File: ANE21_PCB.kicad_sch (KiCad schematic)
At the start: 8 parts

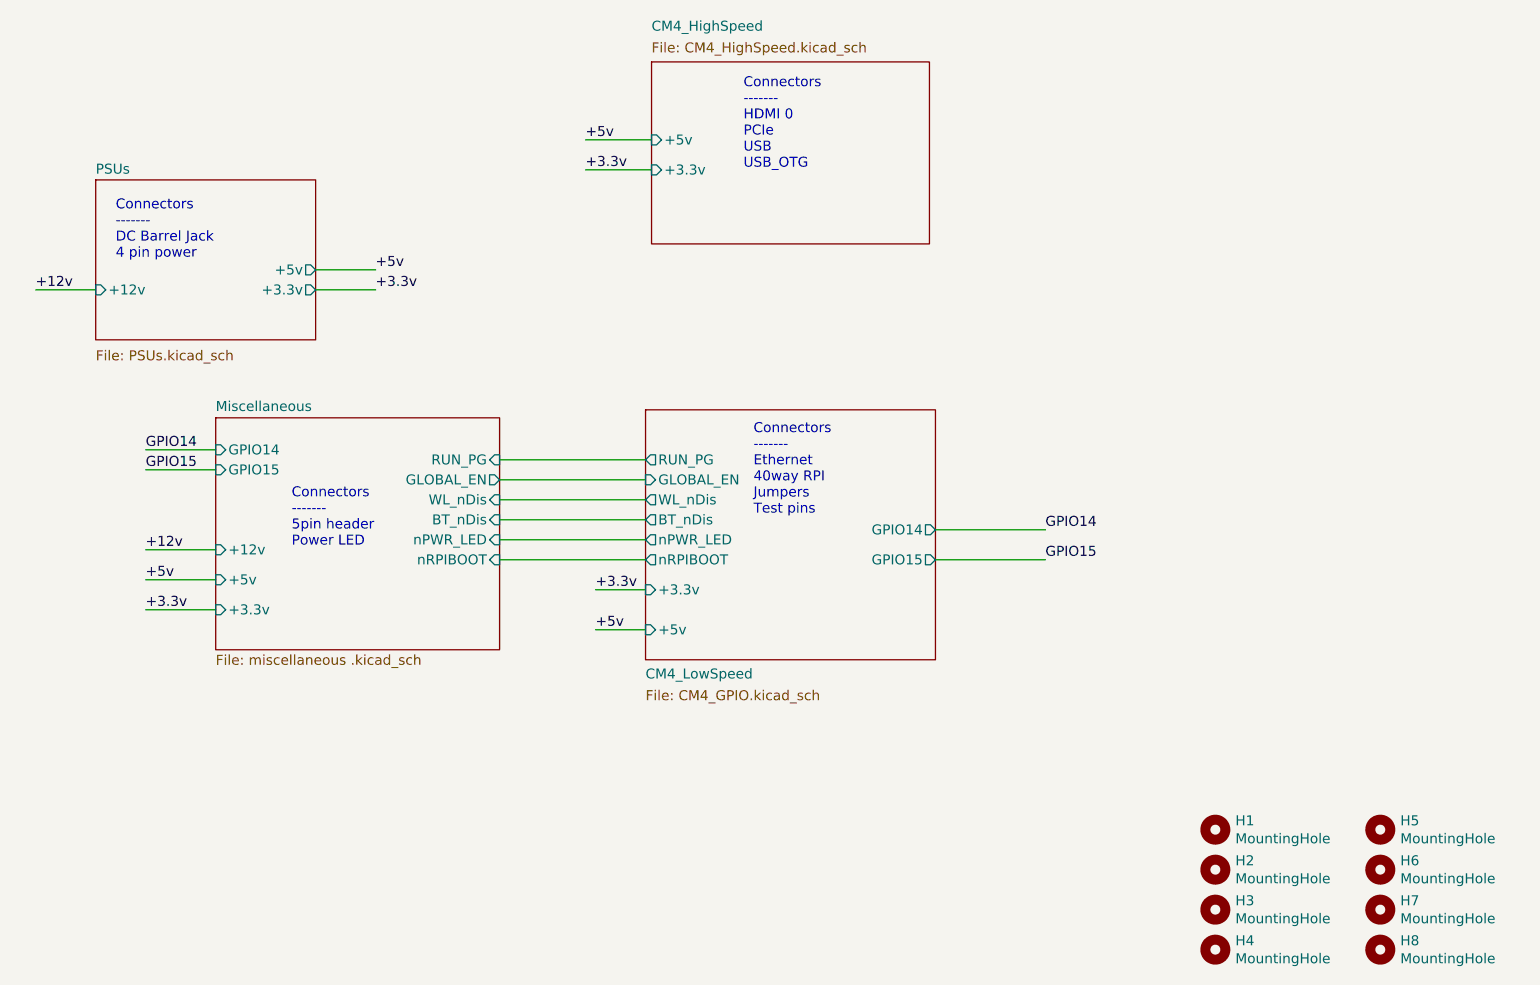
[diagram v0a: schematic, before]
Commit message: Adjusted 3.3v for CM4 3.3v output, PCIe stayed the same.
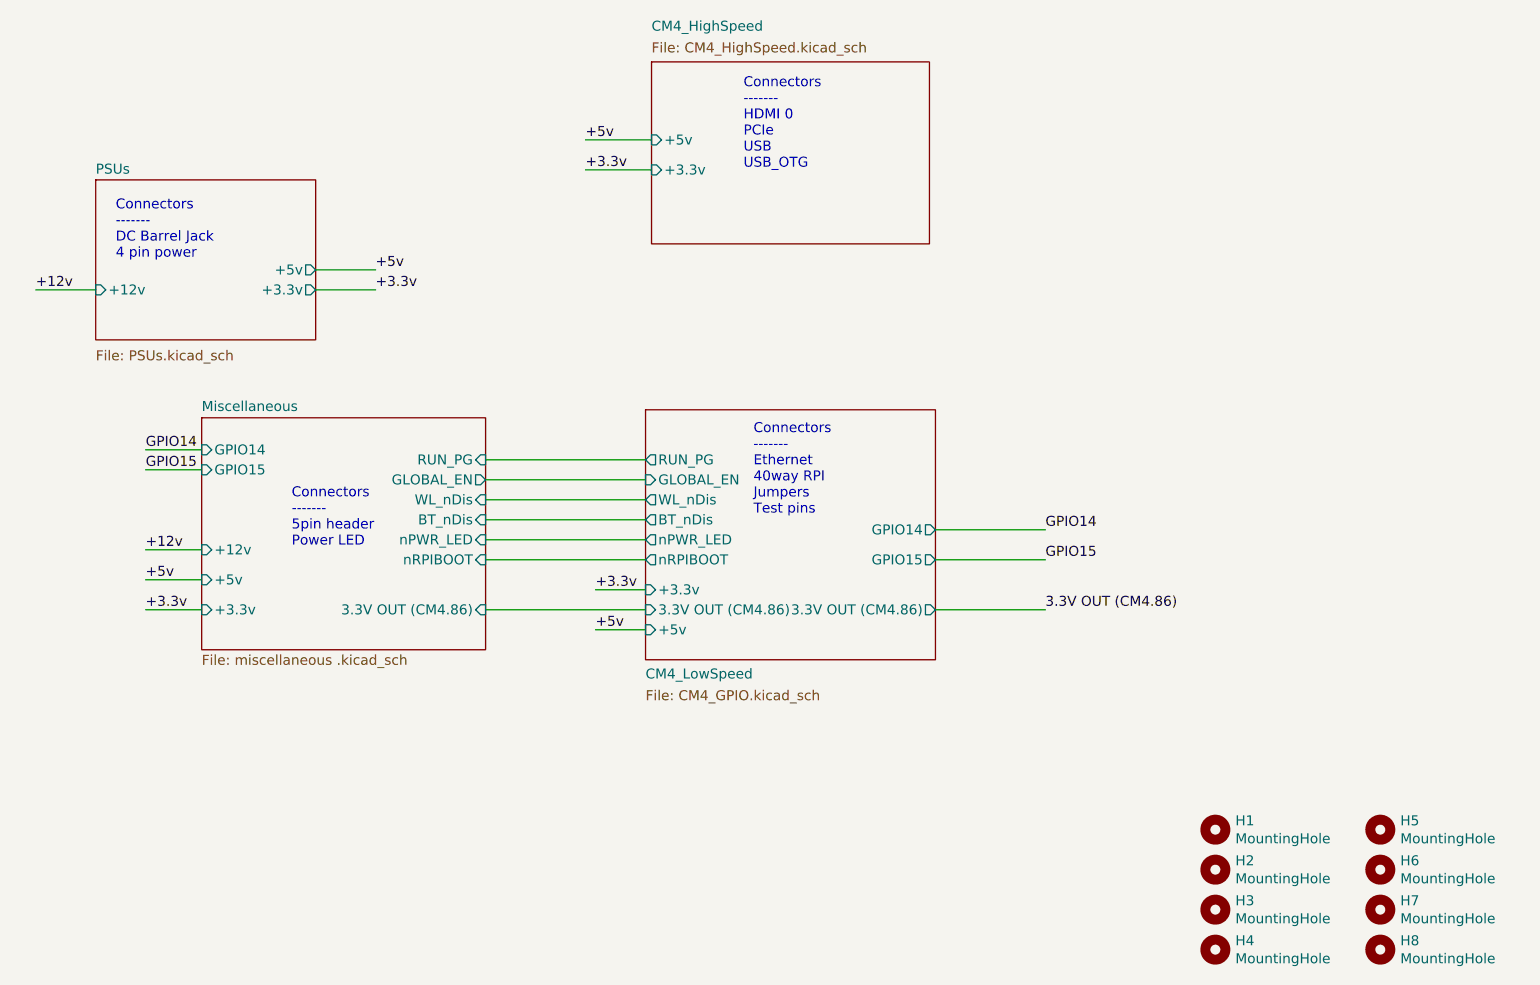
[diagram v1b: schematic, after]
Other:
- sheet CM4_LowSpeed ports: added 3.3V OUT (CM4.86); removed none
- sheet Miscellaneous ports: added 3.3V OUT (CM4.86); removed none
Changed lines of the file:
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@@
 	(wire
 		(pts
-			(xy 43.18 101.6) (xy 52.07 101.6)
-		)
-		(stroke
-			(width 0)
-			(type default)
-		)
-	)
-	(wire
-		(pts
-			(xy 43.18 115.57) (xy 52.07 115.57)
-		)
-		(stroke
-			(width 0)
-			(type default)
-		)
-	)
-	(wire
-		(pts
-			(xy 43.18 111.76) (xy 52.07 111.76)
+			(xy 43.18 101.6) (xy 50.292 101.6)
+		)
+		(stroke
+			(width 0)
+			(type default)
+		)
+	)
+	(wire
+		(pts
+			(xy 43.18 115.57) (xy 50.292 115.57)
+		)
+		(stroke
+			(width 0)
+			(type default)
+		)
+	)
+	(wire
+		(pts
+			(xy 43.18 111.76) (xy 50.292 111.76)
+		)
+		(stroke
+			(width 0)
+			(type default)
+		)
+	)
+	(wire
+		(pts
+			(xy 86.36 119.38) (xy 106.68 119.38)
 		)
 		(stroke
@@
 	(wire
 		(pts
-			(xy 88.138 110.49) (xy 106.68 110.49)
+			(xy 86.36 110.49) (xy 106.68 110.49)
 		)
 		(stroke
@@
 	(wire
 		(pts
-			(xy 88.138 100.33) (xy 106.68 100.33)
+			(xy 86.36 100.33) (xy 106.68 100.33)
 		)
 		(stroke
@@
 	(wire
 		(pts
-			(xy 88.138 113.03) (xy 106.68 113.03)
+			(xy 86.36 113.03) (xy 106.68 113.03)
 		)
 		(stroke
@@
 	(wire
 		(pts
-			(xy 88.138 107.95) (xy 106.68 107.95)
-		)
-		(stroke
-			(width 0)
-			(type default)
-		)
-	)
-	(wire
-		(pts
-			(xy 43.18 119.38) (xy 52.07 119.38)
-		)
-		(stroke
-			(width 0)
-			(type default)
-		)
-	)
-	(wire
-		(pts
-			(xy 43.18 99.06) (xy 52.07 99.06)
+			(xy 86.36 107.95) (xy 106.68 107.95)
+		)
+		(stroke
+			(width 0)
+			(type default)
+		)
+	)
+	(wire
+		(pts
+			(xy 43.18 119.38) (xy 50.292 119.38)
+		)
+		(stroke
+			(width 0)
+			(type default)
+		)
+	)
+	(wire
+		(pts
+			(xy 43.18 99.06) (xy 50.292 99.06)
 		)
 		(stroke
@@
 	(wire
 		(pts
-			(xy 88.138 102.87) (xy 106.68 102.87)
-		)
-		(stroke
-			(width 0)
-			(type default)
-		)
-	)
-	(wire
-		(pts
-			(xy 88.138 105.41) (xy 106.68 105.41)
+			(xy 86.36 102.87) (xy 106.68 102.87)
+		)
+		(stroke
+			(width 0)
+			(type default)
+		)
+	)
+	(wire
+		(pts
+			(xy 143.51 119.38) (xy 157.48 119.38)
+		)
+		(stroke
+			(width 0)
+			(type default)
+		)
+	)
+	(wire
+		(pts
+			(xy 86.36 105.41) (xy 106.68 105.41)
 		)
 		(stroke
@@
 	(label "+3.3v"
 		(at 72.39 78.74 0)
+		(effects
+			(font
+				(size 1.27 1.27)
+			)
+			(justify left bottom)
+		)
+	)
+	(label "3.3V OUT (CM4.86)"
+		(at 157.48 119.38 0)
 		(effects
 			(font
@@
 	)
 	(sheet
-		(at 52.07 94.996)
+		(at 50.292 94.996)
 		(size 36.068 29.464)
 		(exclude_from_sim no)
@@
 		)
 		(property "Sheetname" "Miscellaneous"
-			(at 52.07 94.2844 0)
+			(at 50.292 94.2844 0)
 			(effects
 				(font
@@
 		)
 		(property "Sheetfile" "miscellaneous .kicad_sch"
-			(at 52.07 125.0446 0)
+			(at 50.292 125.0446 0)
 			(effects
 				(font
@@
 		)
 		(pin "BT_nDis" input
-			(at 88.138 107.95 0)
+			(at 86.36 107.95 0)
 			(effects
 				(font
@@
 		)
 		(pin "GLOBAL_EN" output
-			(at 88.138 102.87 0)
+			(at 86.36 102.87 0)
 			(effects
 				(font
@@
 		)
 		(pin "WL_nDis" input
-			(at 88.138 105.41 0)
+			(at 86.36 105.41 0)
 			(effects
 				(font
@@
 		)
 		(pin "nPWR_LED" input
-			(at 88.138 110.49 0)
+			(at 86.36 110.49 0)
 			(effects
 				(font
@@
 		)
 		(pin "nRPIBOOT" input
-			(at 88.138 113.03 0)
+			(at 86.36 113.03 0)
 			(effects
 				(font
@@
 		)
 		(pin "RUN_PG" input
-			(at 88.138 100.33 0)
+			(at 86.36 100.33 0)
 			(effects
 				(font
@@
 		)
 		(pin "+3.3v" input
-			(at 52.07 119.38 180)
+			(at 50.292 119.38 180)
 			(effects
 				(font
@@
 		)
 		(pin "+5v" input
-			(at 52.07 115.57 180)
+			(at 50.292 115.57 180)
 			(effects
 				(font
@@
 		)
 		(pin "+12v" input
-			(at 52.07 111.76 180)
+			(at 50.292 111.76 180)
 			(effects
 				(font
@@
 		)
 		(pin "GPIO14" input
-			(at 52.07 99.06 180)
+			(at 50.292 99.06 180)
 			(effects
 				(font
@@
 		)
 		(pin "GPIO15" input
-			(at 52.07 101.6 180)
-			(effects
-				(font
-					(size 1.27 1.27)
-				)
-				(justify left)
+			(at 50.292 101.6 180)
+			(effects
+				(font
+					(size 1.27 1.27)
+				)
+				(justify left)
+			)
+		)
+		(pin "3.3V OUT (CM4.86)" input
+			(at 86.36 119.38 0)
+			(effects
+				(font
+					(size 1.27 1.27)
+				)
+				(justify right)
 			)
 		)
@@
 			)
 		)
+		(pin "3.3V OUT (CM4.86)" output
+			(at 143.51 119.38 0)
+			(effects
+				(font
+					(size 1.27 1.27)
+				)
+				(justify right)
+			)
+		)
+		(pin "3.3V OUT (CM4.86)" input
+			(at 106.68 119.38 180)
+			(effects
+				(font
+					(size 1.27 1.27)
+				)
+				(justify left)
+			)
+		)

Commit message: Changed quite a bit, PCB smoll now
Redid all traces, replaced HUSB238 with ch224k, made PCB even smaller.
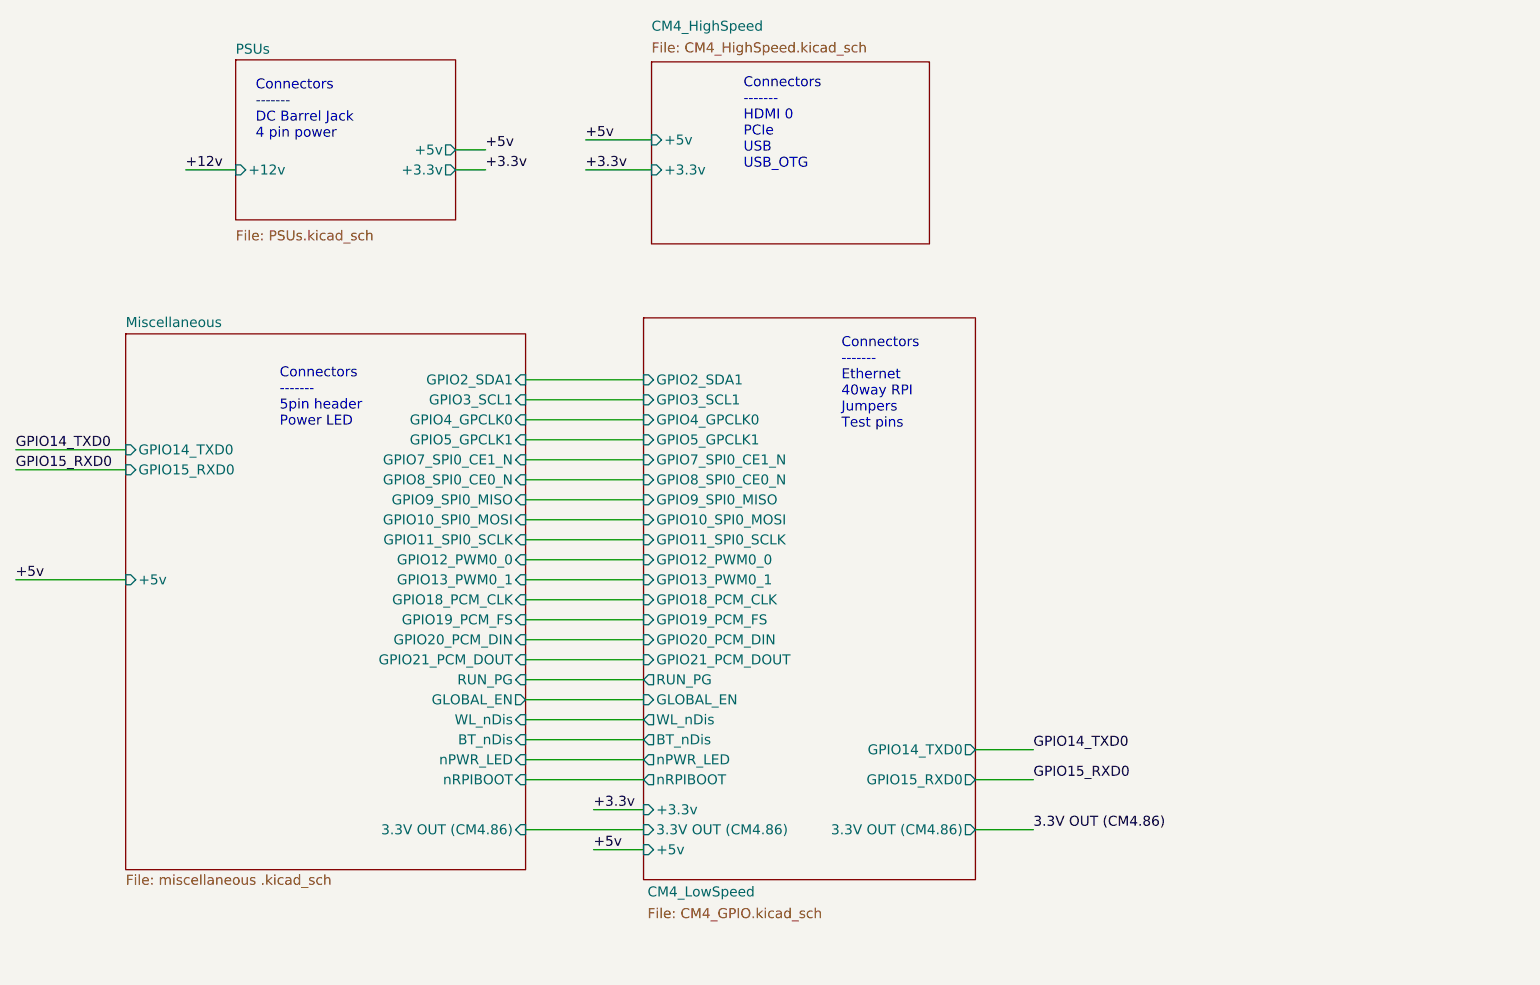
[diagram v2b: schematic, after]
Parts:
- removed H1, H2, H3, H4, H5, H6, H7, H8: MountingHole, MountingHole:MountingHole_2.7mm_M2.5, symbol Mechanical:MountingHole
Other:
- sheet CM4_LowSpeed ports: added GPIO10_SPI0_MOSI, GPIO11_SPI0_SCLK, GPIO12_PWM0_0, GPIO13_PWM0_1, GPIO14_TXD0, GPIO15_RXD0, GPIO18_PCM_CLK, GPIO19_PCM_FS, GPIO20_PCM_DIN, GPIO21_PCM_DOUT, GPIO2_SDA1, GPIO3_SCL1, GPIO4_GPCLK0, GPIO5_GPCLK1, GPIO7_SPI0_CE1_N, GPIO8_SPI0_CE0_N, GPIO9_SPI0_MISO; removed GPIO14, GPIO15
- sheet Miscellaneous ports: added GPIO10_SPI0_MOSI, GPIO11_SPI0_SCLK, GPIO12_PWM0_0, GPIO13_PWM0_1, GPIO14_TXD0, GPIO15_RXD0, GPIO18_PCM_CLK, GPIO19_PCM_FS, GPIO20_PCM_DIN, GPIO21_PCM_DOUT, GPIO2_SDA1, GPIO3_SCL1, GPIO4_GPCLK0, GPIO5_GPCLK1, GPIO7_SPI0_CE1_N, GPIO8_SPI0_CE0_N, GPIO9_SPI0_MISO; removed +12v, +3.3v, GPIO14, GPIO15
